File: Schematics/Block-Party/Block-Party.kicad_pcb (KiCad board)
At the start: 2 copper layers, 15.2 x 15.2 mm, 10 parts

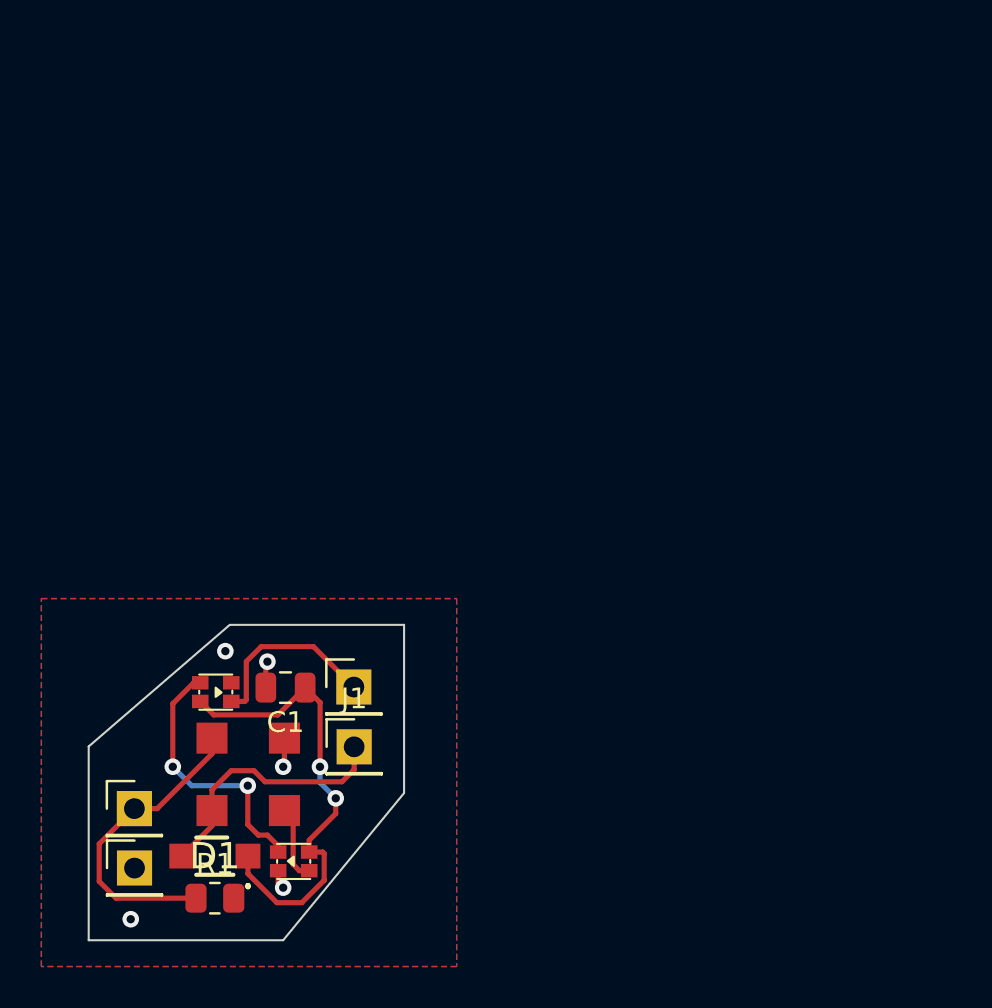
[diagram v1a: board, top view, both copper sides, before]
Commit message: Finished touch up details for the bottom block board
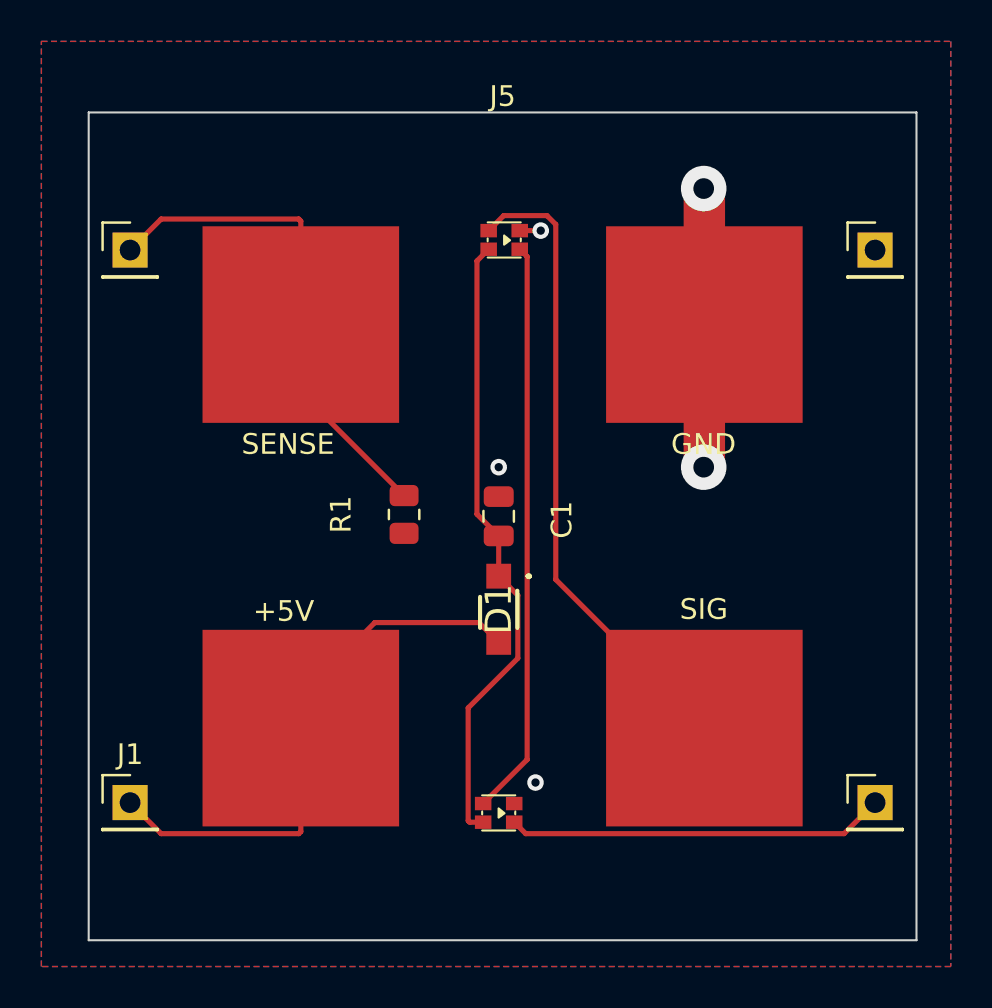
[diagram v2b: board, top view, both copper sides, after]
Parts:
- moved J4 46.6 mm to (177.7, 65.7)
- moved LED2 31.7 mm to (159.8, 65.2), turned to 180 degrees
- moved J3 27.0 mm to (141.7, 65.7)
- moved J2 25.8 mm to (177.7, 92.4)
- moved R1 20.7 mm to (154.9, 78.5), turned to -90 degrees
- moved D1 18.2 mm to (159.5, 83.1), turned to -90 degrees
- moved J5 17.2 mm to (159.7, 79.1)
- moved LED1 14.9 mm to (159.5, 92.9)
- moved C1 13.2 mm to (159.5, 78.6), turned to 90 degrees
- moved J1 11.2 mm to (141.7, 92.4)
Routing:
- net DIN: track 3.68 -> 31.0 mm
- net Net-(LED1-DI): track 12.9 -> 27.8 mm, vias 2 -> 0
- net +5V: track 12.6 -> 26.9 mm
- net GND: track 3.61 -> 14.5 mm
- net SENSE: track 14.8 -> 24.2 mm
- net DOUT: track 8.91 -> 18.3 mm
- net D5V: track 22.6 -> 30.4 mm, vias 2 -> 0
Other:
- board size 15.2 x 15.2 mm -> 40 x 40 mm

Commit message: Finished v1.0 of the PCBs
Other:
- board text added: "+5V"
- board text added: "DIN"
- board text added: "GND"
- board text added: "SENSE"
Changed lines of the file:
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@@
     (fp_rect (start 3.75 4.75) (end 15.75 14.75)
       (stroke (width 0.05) (type default)) (fill none) (layer "F.CrtYd"))
+    (pad "" thru_hole oval (at -15.15 -9.75) (size 1.05 9.5) (drill oval 1 9.75) (layers "*.Mask")
+      (pinfunction "HOLE") (pintype "output+no_connect") (thermal_bridge_angle 45))
+    (pad "" thru_hole oval (at -15.15 9.75) (size 1.05 9.5) (drill oval 1 9.75) (layers "*.Mask")
+      (pinfunction "HOLE") (pintype "output+no_connect") (thermal_bridge_angle 45))
+    (pad "" thru_hole oval (at -4.35 -9.75) (size 1.05 9.5) (drill oval 1 9.75) (layers "*.Mask")
+      (pinfunction "HOLE") (pintype "output+no_connect") (thermal_bridge_angle 45))
+    (pad "" thru_hole oval (at -4.35 9.75) (size 1.05 9.5) (drill oval 1 9.75) (layers "*.Mask")
+      (pinfunction "HOLE") (pintype "output+no_connect") (thermal_bridge_angle 45))
+    (pad "" thru_hole oval (at 4.35 -9.75) (size 1.05 9.5) (drill oval 1 9.75) (layers "*.Mask")
+      (pinfunction "HOLE") (pintype "output+no_connect") (thermal_bridge_angle 45))
+    (pad "" thru_hole oval (at 4.35 9.75) (size 1.05 9.5) (drill oval 1 9.75) (layers "*.Mask")
+      (pinfunction "HOLE") (pintype "output+no_connect") (thermal_bridge_angle 45))
+    (pad "" thru_hole oval (at 15.15 -9.75) (size 1.05 9.5) (drill oval 1 9.75) (layers "*.Mask")
+      (pinfunction "HOLE") (pintype "output+no_connect") (thermal_bridge_angle 45))
+    (pad "" thru_hole oval (at 15.15 9.75) (size 1.05 9.5) (drill oval 1 9.75) (layers "*.Mask")
+      (pinfunction "HOLE") (pintype "output+no_connect") (thermal_bridge_angle 45))
     (pad "1" smd rect (at 9.75 -9.75) (size 9.5 9.5) (layers "F.Cu" "F.Paste" "F.Mask")
       (net 2 "GND") (pinfunction "GND") (pintype "power_in") (thermal_bridge_angle 45))
@@
     (pad "4" smd rect (at -9.75 9.75) (size 9.5 9.5) (layers "F.Cu" "F.Paste" "F.Mask")
       (net 3 "+5V") (pinfunction "+5V") (pintype "power_in") (thermal_bridge_angle 45))
-    (pad "5" thru_hole oval (at -15.15 -9.75) (size 1.05 9.5) (drill oval 1 9.75) (layers "*.Mask")
-      (pinfunction "HOLE") (pintype "output+no_connect") (thermal_bridge_angle 45))
-    (pad "5" thru_hole oval (at -15.15 9.75) (size 1.05 9.5) (drill oval 1 9.75) (layers "*.Mask")
-      (pinfunction "HOLE") (pintype "output+no_connect") (thermal_bridge_angle 45))
-    (pad "5" thru_hole oval (at -4.35 -9.75) (size 1.05 9.5) (drill oval 1 9.75) (layers "*.Mask")
-      (pinfunction "HOLE") (pintype "output+no_connect") (thermal_bridge_angle 45))
-    (pad "5" thru_hole oval (at -4.35 9.75) (size 1.05 9.5) (drill oval 1 9.75) (layers "*.Mask")
-      (pinfunction "HOLE") (pintype "output+no_connect") (thermal_bridge_angle 45))
-    (pad "5" thru_hole oval (at 4.35 -9.75) (size 1.05 9.5) (drill oval 1 9.75) (layers "*.Mask")
-      (pinfunction "HOLE") (pintype "output+no_connect") (thermal_bridge_angle 45))
-    (pad "5" thru_hole oval (at 4.35 9.75) (size 1.05 9.5) (drill oval 1 9.75) (layers "*.Mask")
-      (pinfunction "HOLE") (pintype "output+no_connect") (thermal_bridge_angle 45))
-    (pad "5" thru_hole oval (at 15.15 -9.75) (size 1.05 9.5) (drill oval 1 9.75) (layers "*.Mask")
-      (pinfunction "HOLE") (pintype "output+no_connect") (thermal_bridge_angle 45))
-    (pad "5" thru_hole oval (at 15.15 9.75) (size 1.05 9.5) (drill oval 1 9.75) (layers "*.Mask")
-      (pinfunction "HOLE") (pintype "output+no_connect") (thermal_bridge_angle 45))
   )
   (gr_rect (start 139.7 59.06) (end 179.7 99.06)
     (stroke (width 0.1) (type default)) (fill none) (layer "Edge.Cuts"))
+  (gr_text "GND" (at 170.942 75.692) (layer "B.SilkS")
+    (effects (font (size 1 1) (thickness 0.15)) (justify left bottom mirror))
+  )
+  (gr_text "+5V" (at 151.13 83.82) (layer "B.SilkS")
+    (effects (font (size 1 1) (thickness 0.15)) (justify left bottom mirror))
+  )
+  (gr_text "SENSE" (at 152.146 75.692) (layer "B.SilkS")
+    (effects (font (size 1 1) (thickness 0.15)) (justify left bottom mirror))
+  )
+  (gr_text "DIN" (at 170.942 83.566) (layer "B.SilkS")
+    (effects (font (size 1 1) (thickness 0.15)) (justify left bottom mirror))
+  )
   (segment (start 158.037 87.835) (end 160.437 85.435) (width 0.25) (layer "F.Cu") (net 1))
   (segment (start 160.437 85.435) (end 160.437 82.393259) (width 0.25) (layer "F.Cu") (net 1))

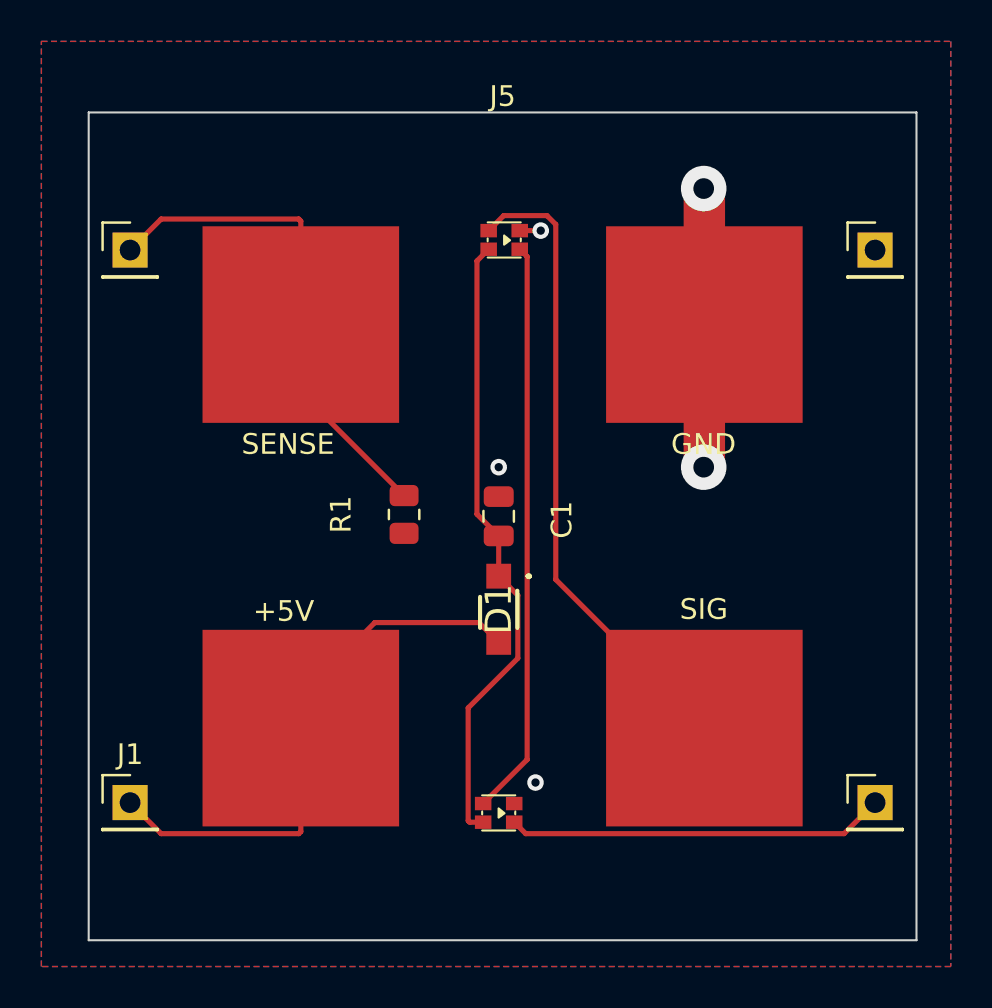
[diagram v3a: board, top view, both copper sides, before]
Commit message: Flipped the bottom pads to be the correct orientation
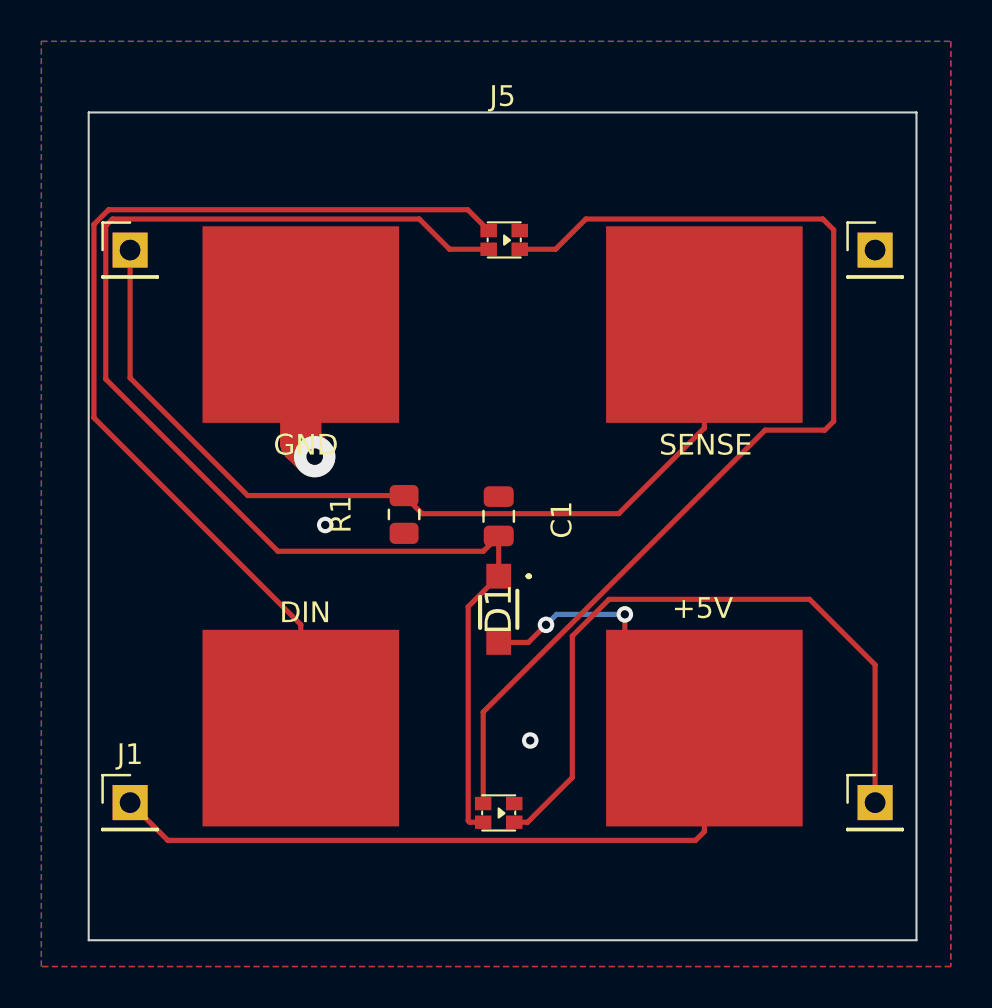
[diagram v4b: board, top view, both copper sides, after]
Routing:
- net D5V: track 30.4 -> 64.5 mm
- net Net-(LED1-DI): track 27.8 -> 52.4 mm
- net +5V: track 26.9 -> 47.4 mm, vias 0 -> 2
- net SENSE: track 24.2 -> 43.4 mm
- net DIN: track 31.0 -> 48.3 mm
- net DOUT: track 18.3 -> 33.9 mm
- net GND: track 14.5 -> 6.66 mm, vias 5 -> 3
